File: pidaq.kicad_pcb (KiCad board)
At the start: 2 copper layers, 95.2 x 95.3 mm, 51 parts, among them J1 Screw_Terminal_01x10, J2 Screw_Terminal_01x10, J3 Screw_Terminal_01x08, J4 Screw_Terminal_01x08, J5 Conn_01x03_Male, J6 Conn_01x08_Female, J7 Screw_Terminal_01x04, J8 Conn_01x03_Male, U1 LTC2984CLX-DNP, U2 LTC2449CUHF, U3 SN74LV1T34DCKR, U4 INA126U

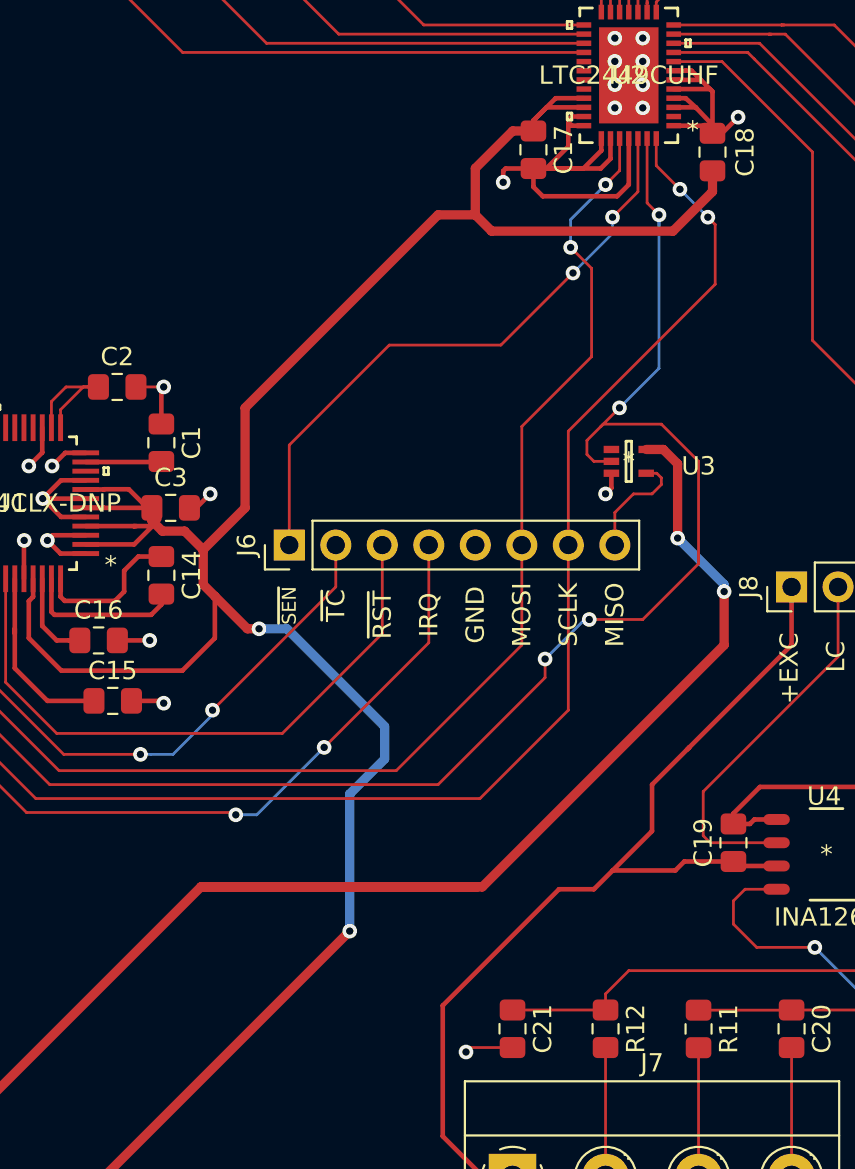
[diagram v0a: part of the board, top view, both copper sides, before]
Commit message: moved vias into pads
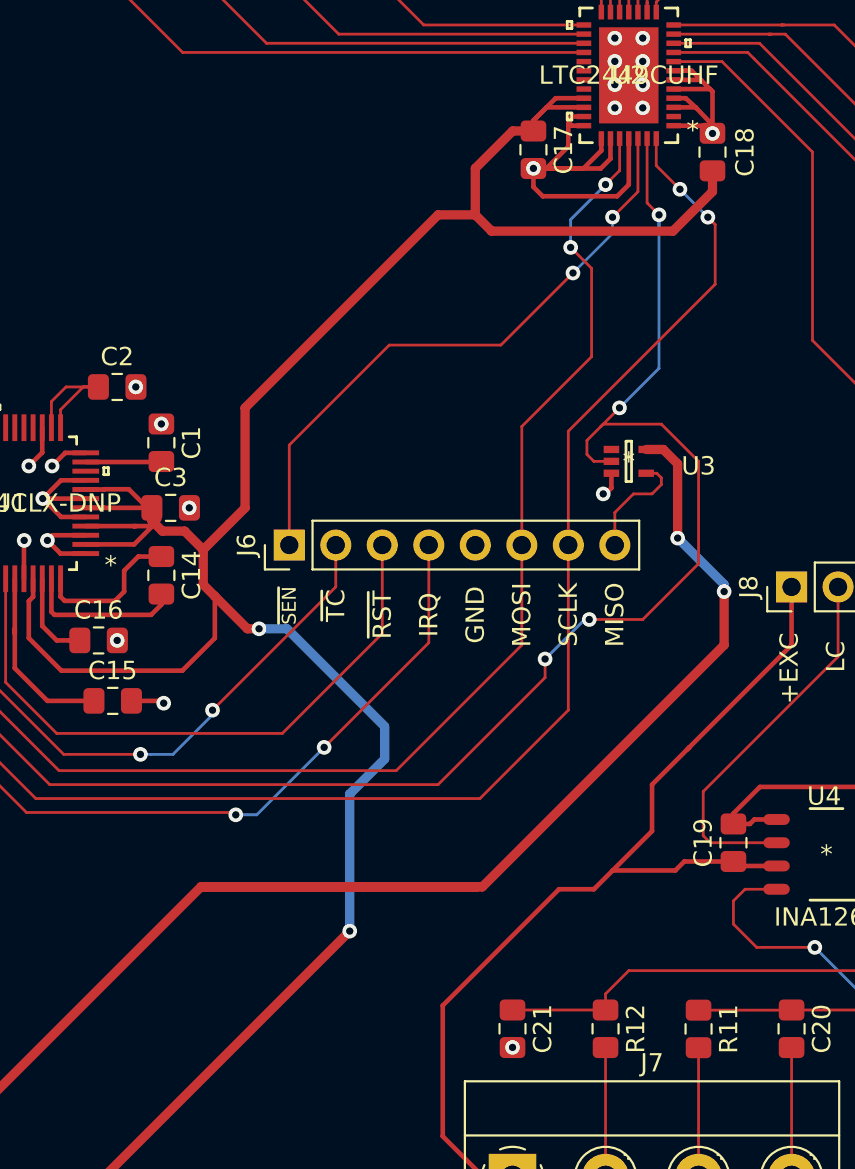
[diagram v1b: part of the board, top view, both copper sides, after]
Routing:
- net GND: track 156.4 -> 143.7 mm, vias 23 -> 24
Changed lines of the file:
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@@
     (thickness 1.6)
     (drawings 61)
-    (tracks 537)
+    (tracks 528)
     (zones 0)
     (modules 51)
@@
   )
   (setup
-    (last_trace_width 0.1524)
+    (last_trace_width 0.15)
     (user_trace_width 0.1524)
     (user_trace_width 0.254)
@@
   (segment (start 80.295634 124.46) (end 84.065 124.46) (width 0.1524) (layer F.Cu) (net 2))
   (segment (start 78.74 124.46) (end 80.295634 124.46) (width 0.1524) (layer F.Cu) (net 2))
-  (via (at 107.95 93.218) (size 0.8) (drill 0.4) (layers F.Cu B.Cu) (net 2))
-  (segment (start 106.435 93.218) (end 107.95 93.218) (width 0.1524) (layer F.Cu) (net 2))
+  (via (at 106.426 93.218) (size 0.8) (drill 0.4) (layers F.Cu B.Cu) (net 2))
   (segment (start 130.2412 78.450001) (end 130.048 78.643201) (width 0.254) (layer F.Cu) (net 2))
   (segment (start 130.8976 78.450001) (end 130.2412 78.450001) (width 0.254) (layer F.Cu) (net 2))
@@
   (segment (start 135.8024 78.95) (end 137.506 78.95) (width 0.254) (layer F.Cu) (net 2))
   (segment (start 137.922 79.366) (end 138.439 79.366) (width 0.254) (layer F.Cu) (net 2))
-  (via (at 139.319 78.486) (size 0.8) (drill 0.4) (layers F.Cu B.Cu) (net 2))
-  (segment (start 138.439 79.366) (end 139.319 78.486) (width 0.254) (layer F.Cu) (net 2))
-  (via (at 126.492 82.042) (size 0.8) (drill 0.4) (layers F.Cu B.Cu) (net 2))
-  (segment (start 128.143 81.289) (end 126.628 81.289) (width 0.254) (layer F.Cu) (net 2))
-  (via (at 107.188 107.061) (size 0.8) (drill 0.4) (layers F.Cu B.Cu) (net 2))
-  (segment (start 105.419 107.061) (end 107.188 107.061) (width 0.254) (layer F.Cu) (net 2))
-  (segment (start 107.823 93.345) (end 107.95 93.218) (width 0.254) (layer F.Cu) (net 2))
-  (segment (start 107.823 95.241) (end 107.823 93.345) (width 0.254) (layer F.Cu) (net 2))
-  (via (at 132.08 99.06) (size 0.8) (drill 0.4) (layers F.Cu B.Cu) (net 2))
+  (via (at 137.922 79.375) (size 0.8) (drill 0.4) (layers F.Cu B.Cu) (net 2))
+  (via (at 128.143 81.28) (size 0.8) (drill 0.4) (layers F.Cu B.Cu) (net 2))
+  (via (at 105.41 107.061) (size 0.8) (drill 0.4) (layers F.Cu B.Cu) (net 2))
+  (segment (start 107.823 95.241) (end 107.823 95.241) (width 0.254) (layer F.Cu) (net 2))
+  (via (at 131.953 99.06) (size 0.8) (drill 0.4) (layers F.Cu B.Cu) (net 2))
   (segment (start 132.400002 97.931999) (end 132.400002 98.739998) (width 0.254) (layer F.Cu) (net 2))
   (segment (start 132.400002 98.739998) (end 132.08 99.06) (width 0.254) (layer F.Cu) (net 2))
@@
   (segment (start 107.823 110.363) (end 107.95 110.49) (width 0.254) (layer F.Cu) (net 2))
   (segment (start 109.356 99.822) (end 109.728 99.822) (width 0.254) (layer F.Cu) (net 2))
-  (via (at 110.49 99.06) (size 0.8) (drill 0.4) (layers F.Cu B.Cu) (net 2))
-  (segment (start 109.728 99.822) (end 110.49 99.06) (width 0.254) (layer F.Cu) (net 2))
+  (via (at 109.347 99.822) (size 0.8) (drill 0.4) (layers F.Cu B.Cu) (net 2))
   (segment (start 100.318001 103.693001) (end 100.318001 101.611999) (width 0.254) (layer F.Cu) (net 2))
   (via (at 100.33 101.6) (size 0.8) (drill 0.4) (layers F.Cu B.Cu) (net 2))
@@
   (segment (start 103.693001 96.818) (end 102.572 96.818) (width 0.254) (layer F.Cu) (net 2))
   (segment (start 102.572 96.818) (end 101.854 97.536) (width 0.254) (layer F.Cu) (net 2))
-  (segment (start 126.492 81.425) (end 126.492 82.042) (width 0.254) (layer F.Cu) (net 2))
-  (segment (start 126.628 81.289) (end 126.492 81.425) (width 0.254) (layer F.Cu) (net 2))
   (segment (start 142.24 136.398) (end 142.24 129.295) (width 0.1524) (layer F.Cu) (net 2))
-  (via (at 124.46 129.54) (size 0.8) (drill 0.4) (layers F.Cu B.Cu) (net 2))
-  (segment (start 127 129.295) (end 124.705 129.295) (width 0.1524) (layer F.Cu) (net 2))
-  (segment (start 124.705 129.295) (end 124.46 129.54) (width 0.1524) (layer F.Cu) (net 2))
+  (via (at 127 129.286) (size 0.8) (drill 0.4) (layers F.Cu B.Cu) (net 2))
   (segment (start 140.208 116.84) (end 139.963 117.085) (width 0.254) (layer F.Cu) (net 2))
   (segment (start 139.963 117.085) (end 139.065 117.085) (width 0.254) (layer F.Cu) (net 2))
@@
   (segment (start 147.849 116.84) (end 148.209 116.48) (width 0.254) (layer F.Cu) (net 2))
   (segment (start 148.209 115.824) (end 147.447 115.062) (width 0.254) (layer F.Cu) (net 2))
+  (via (at 107.823 95.241) (size 0.8) (drill 0.4) (layers F.Cu B.Cu) (net 2))
   (segment (start 101.818001 95.442999) (end 101.818001 94.015999) (width 0.1524) (layer F.Cu) (net 3))
   (segment (start 102.616 93.218) (end 104.385 93.218) (width 0.1524) (layer F.Cu) (net 3))

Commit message: updated preview
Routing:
- net GND: track 143.7 -> 141.9 mm
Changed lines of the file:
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@@
     (thickness 1.6)
     (drawings 61)
-    (tracks 528)
+    (tracks 526)
     (zones 0)
     (modules 51)
@@
   (segment (start 132.400002 97.931999) (end 132.400002 98.739998) (width 0.254) (layer F.Cu) (net 2))
   (segment (start 132.400002 98.739998) (end 132.08 99.06) (width 0.254) (layer F.Cu) (net 2))
-  (via (at 107.95 110.49) (size 0.8) (drill 0.4) (layers F.Cu B.Cu) (net 2))
-  (segment (start 106.19 110.363) (end 107.823 110.363) (width 0.254) (layer F.Cu) (net 2))
-  (segment (start 107.823 110.363) (end 107.95 110.49) (width 0.254) (layer F.Cu) (net 2))
+  (via (at 106.172 110.363) (size 0.8) (drill 0.4) (layers F.Cu B.Cu) (net 2))
   (segment (start 109.356 99.822) (end 109.728 99.822) (width 0.254) (layer F.Cu) (net 2))
   (via (at 109.347 99.822) (size 0.8) (drill 0.4) (layers F.Cu B.Cu) (net 2))

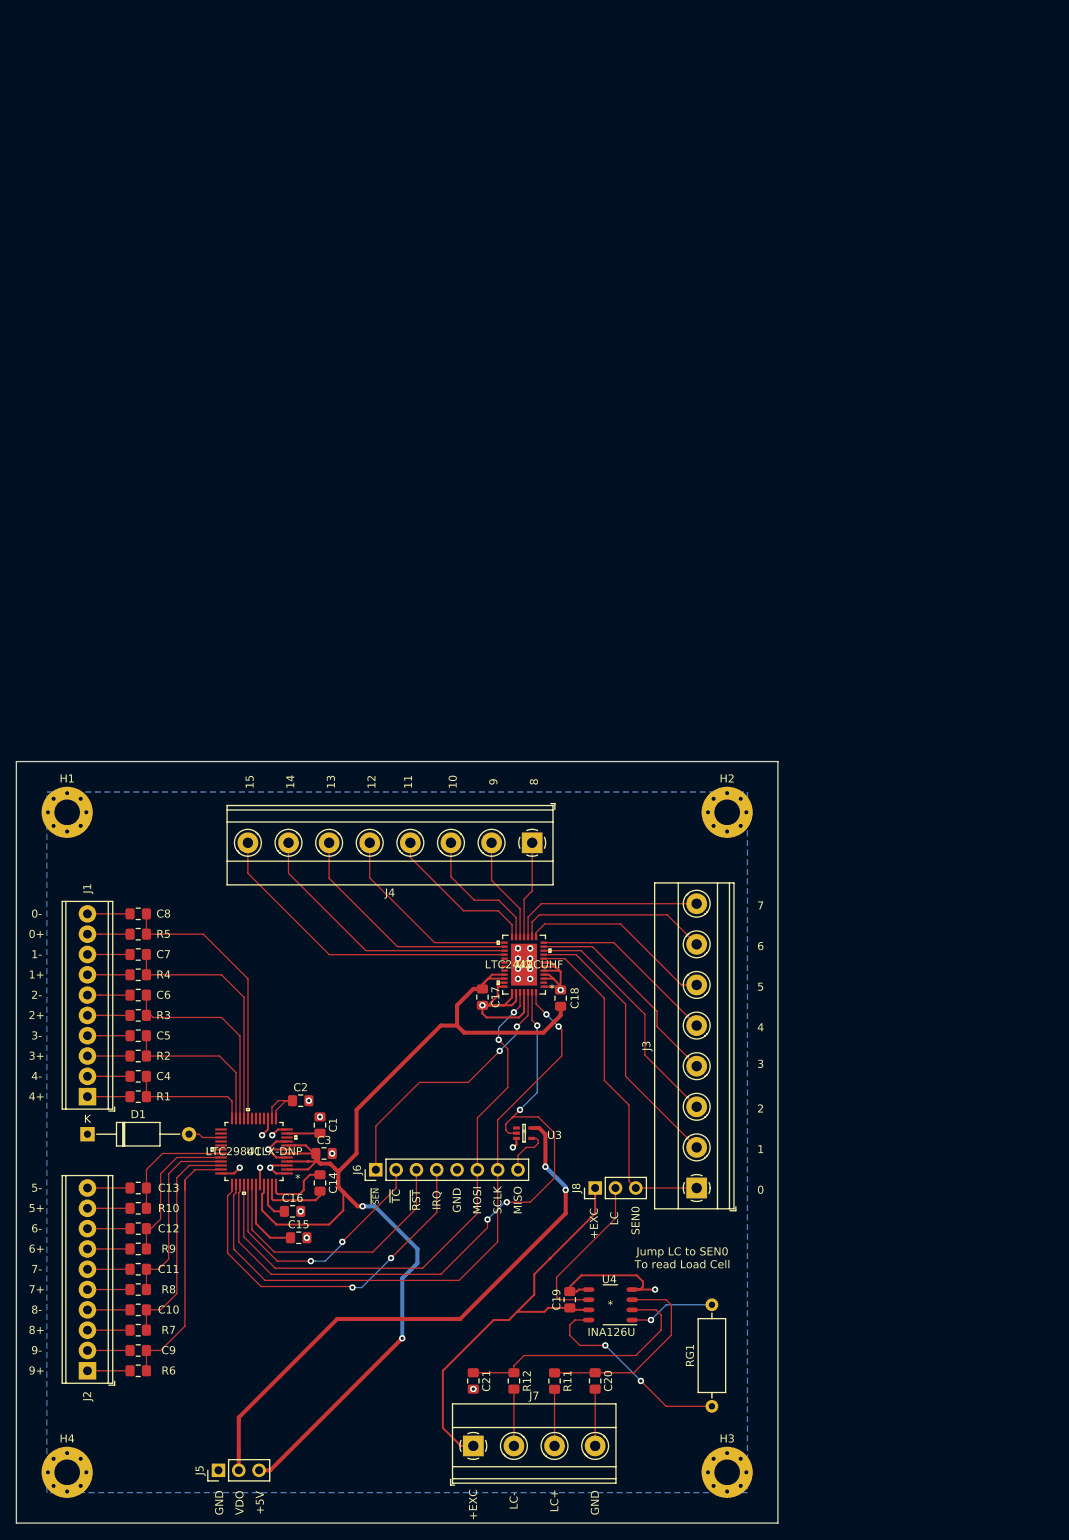
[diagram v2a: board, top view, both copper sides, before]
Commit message: pcb size reduced to 3x3in
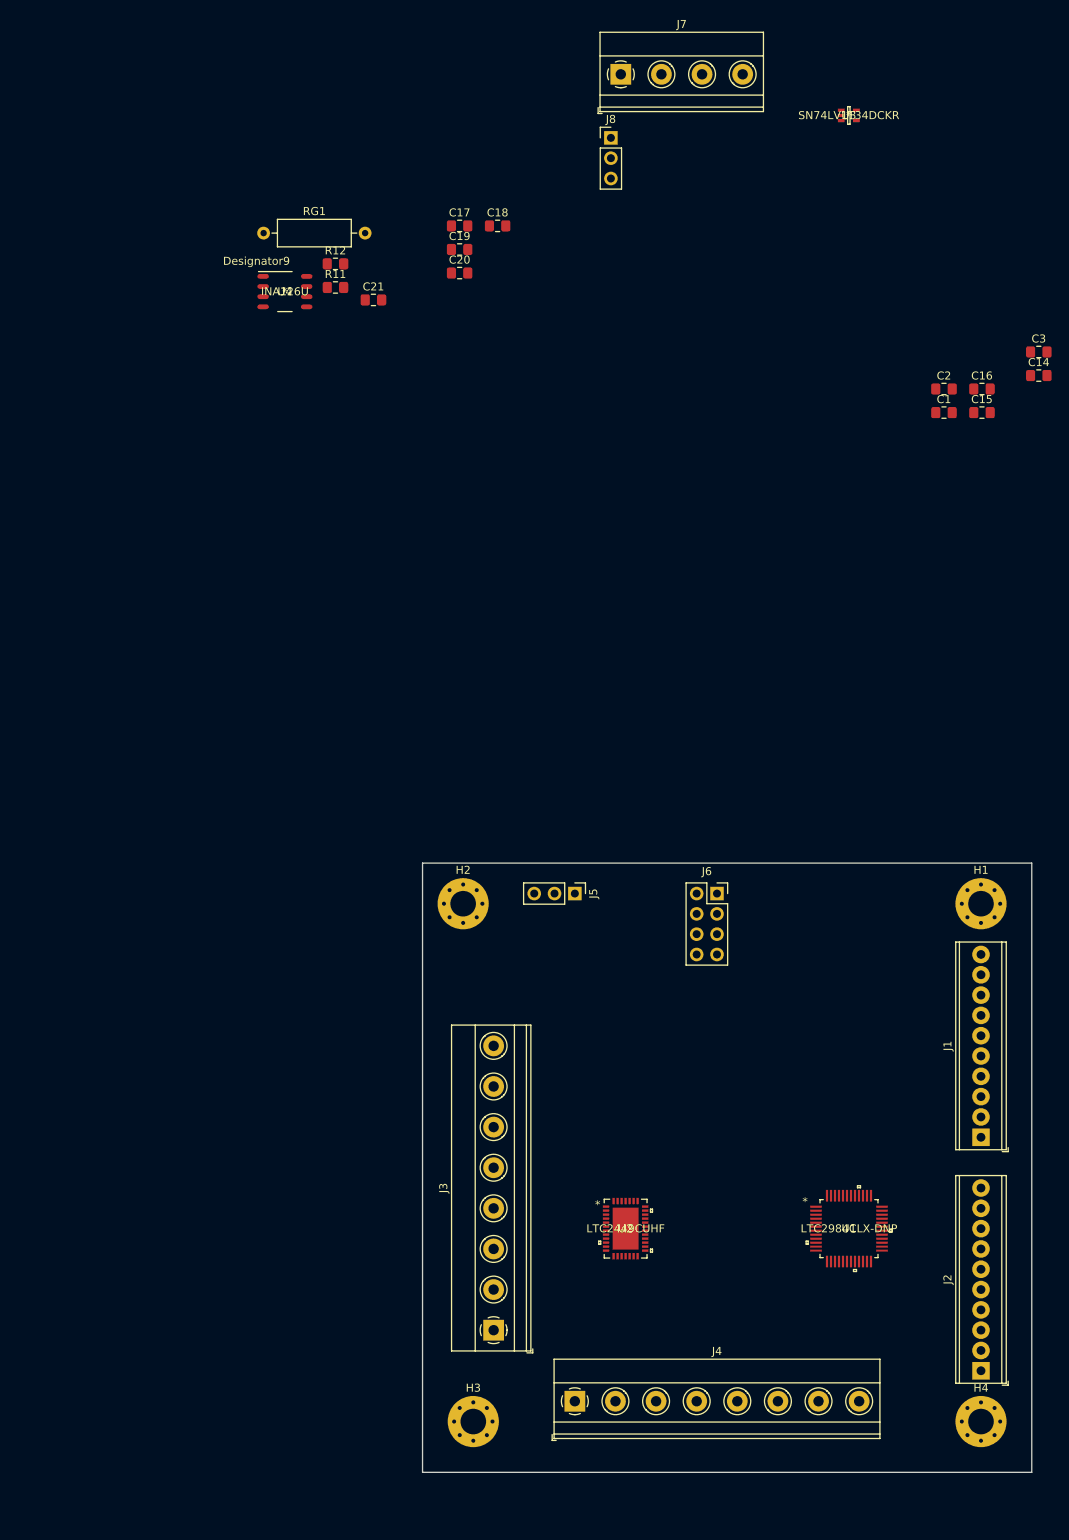
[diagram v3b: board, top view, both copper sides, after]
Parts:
- removed C10, C11, C12, C13, C4, C5, C6, C7, C8, C9: 100pF, Capacitor_SMD:C_0805_2012Metric_Pad1.15x1.40mm_HandSolder
- removed D1: 1N4148, Diode_THT:D_A-405_P12.70mm_Horizontal
- removed R1, R10, R2, R3, R4, R5, R6, R7, R8, R9: 100, Resistor_SMD:R_0805_2012Metric_Pad1.15x1.40mm_HandSolder
- J6: value Conn_01x08_Female -> Conn_02x04_Odd_Even; footprint Connector_PinHeader_2.54mm:PinHeader_1x08_P2.54mm_Vertical -> Connector_PinSocket_2.54mm:PinSocket_2x04_P2.54mm_Vertical
- moved J7 172.5 mm to (145.5, -35.2)
- moved RG1 157.1 mm to (100.8, -15.3), turned to 0 degrees
- moved R12 141.5 mm to (109.8, -11.4), turned to 0 degrees
- moved C20 139.6 mm to (125.3, -10.3), turned to 0 degrees
- moved R11 139.5 mm to (109.8, -8.50), turned to 0 degrees
- moved C21 135.8 mm to (114.5, -6.94), turned to 0 degrees
- moved C14 135.2 mm to (197.7, 2.52), turned to 0 degrees
- moved C3 134.3 mm to (197.7, -0.43)
- moved C16 134.2 mm to (190.6, 4.20)
- moved C15 134.0 mm to (190.6, 7.15)
- moved U3 133.6 mm to (174.0, -30.0)
- moved U4 133.1 mm to (103.4, -7.98), turned to 0 degrees
- moved C19 132.1 mm to (125.3, -13.2), turned to 0 degrees
- moved J8 131.4 mm to (144.2, -27.2), turned to 0 degrees
- moved C2 120.0 mm to (185.9, 4.20)
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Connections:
- J1 pad 1: /thermocouples/TC4RAW -> TC4+
- J1 pad 10: GND -> TC0-
- J1 pad 2: GND -> TC4-
- J1 pad 3: /thermocouples/TC3RAQ -> TC3+
- J1 pad 4: GND -> TC3-
- J1 pad 5: /thermocouples/TC2RAW -> TC2+
- J1 pad 6: GND -> TC2-
- J1 pad 7: /thermocouples/TC1RAW -> TC1+
- J1 pad 8: GND -> TC1-
- J1 pad 9: /thermocouples/TC0RAW -> TC0+
- J2 pad 1: /thermocouples/TC9RAW -> TC9+
- J2 pad 10: GND -> TC5-
- J2 pad 2: GND -> TC9-
- J2 pad 3: /thermocouples/TC8RAW -> TC8+
- J2 pad 4: GND -> TC8-
- J2 pad 5: /thermocouples/TC7RAW -> TC7+
- J2 pad 6: GND -> TC7-
- J2 pad 7: /thermocouples/TC6RAW -> TC6+
- J2 pad 8: GND -> TC6-
- J2 pad 9: /thermocouples/TC5RAW -> TC5+
- J6 pad 1: ~SEN -> GND
- J6 pad 2: ~TC -> MOSI
- J6 pad 3: ~RST -> (no net)
- J6 pad 4: IRQ -> /MISO_SAFE
- J6 pad 5: GND -> ~SEN
- J6 pad 6: MOSI -> SCLK
- J6 pad 7: SCLK -> ~TC
- J6 pad 8: /MISO_SAFE -> GND
- U1 pad 16: (no net) -> TC0+
- U1 pad 17: (no net) -> TC0-
- U1 pad 18: (no net) -> TC1+
- U1 pad 19: (no net) -> TC1-
- U1 pad 20: TC0+ -> TC2+
- U1 pad 21: TC1+ -> TC2-
- U1 pad 22: TC2+ -> TC3+
- U1 pad 23: TC3+ -> TC3-
- U1 pad 25: (no net) -> TC4-
- U1 pad 26: (no net) -> TC5+
- U1 pad 27: /thermocouples/CJ -> TC5-
- U1 pad 28: (no net) -> TC6+
- U1 pad 29: (no net) -> TC6-
- U1 pad 30: (no net) -> TC7+
- U1 pad 31: TC5+ -> TC7-
- U1 pad 32: TC6+ -> TC8+
- U1 pad 33: TC7+ -> TC8-
- U1 pad 34: TC8+ -> TC9+
- U1 pad 35: TC9+ -> TC9-
- U1 pad 37: IRQ -> (no net)
- U1 pad 42: ~RST -> (no net)
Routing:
- net +5V: track 144.9 -> 0.00 mm, vias 2 -> 0
- net GND: track 141.9 -> 0.00 mm, vias 24 -> 0
- net MISO: track 87.1 -> 0.00 mm, vias 4 -> 0
- net VDOUT: track 86.2 -> 0.00 mm, vias 2 -> 0
- net SCLK: track 80.7 -> 0.00 mm, vias 2 -> 0
- net MOSI: track 71.1 -> 0.00 mm, vias 2 -> 0
- net +EXC: track 53.2 -> 0.00 mm
- net IRQ: track 46.0 -> 0.00 mm, vias 2 -> 0
- net SEN0: track 42.6 -> 0.00 mm
- net SEN15: track 40.1 -> 0.00 mm
- net TC0+: track 35.0 -> 0.00 mm
- net SEN14: track 34.8 -> 0.00 mm
- net ~RST: track 34.5 -> 0.00 mm
- net SEN1: track 34.4 -> 0.00 mm
- net ~SEN: track 33.7 -> 0.00 mm, vias 2 -> 0
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- removed copper zone on B.Cu, net GND
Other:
- board size 95.2 x 95.3 mm -> 76.2 x 76.2 mm
- board text removed: "+5V"
- board text removed: "+EXC"
- board text removed: "0"
- board text removed: "0+"
- board text removed: "0-"
- board text removed: "1"
- board text removed: "1+"
- board text removed: "1-"
- board text removed: "10"
- board text removed: "11"
- board text removed: "12"
- board text removed: "13"
- board text removed: "14"
- board text removed: "15"
- board text removed: "2"
- board text removed: "2+"
- board text removed: "2-"
- board text removed: "3"
- board text removed: "3+"
- board text removed: "3-"
- board text removed: "4"
- board text removed: "4+"
- board text removed: "4-"
- board text removed: "5"
- board text removed: "5+"
- board text removed: "5-"
- board text removed: "6"
- board text removed: "6+"
- board text removed: "6-"
- board text removed: "7"
- board text removed: "7+"
- board text removed: "7-"
- board text removed: "8"
- board text removed: "8+"
- board text removed: "8-"
- board text removed: "9"
- board text removed: "9+"
- board text removed: "9-"
- board text removed: "GND"
- board text removed: "IRQ"
- board text removed: "Jump LC to SEN0 To read Load Cell"
- board text removed: "LC"
- board text removed: "LC+"
- board text removed: "LC-"
- board text removed: "MISO"
- board text removed: "MOSI"
- board text removed: "SCLK"
- board text removed: "SEN0"
- board text removed: "VDO"
- board text removed: "~RST"
- board text removed: "~SEN"
- board text removed: "~TC"
